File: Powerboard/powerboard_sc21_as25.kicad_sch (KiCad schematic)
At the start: 56 parts, among them J2 Conn_01x02_Male, J3 Conn_01x02_Male, J4 Conn_01x08_Male, J9 Conn_Coaxial, Q6 MMDT2222A, Q7 RSJ250P10TL, Q8 RSJ250P10TL, U1 LTC4412xS6, U2 SN65HVD230, U3 ESP32-PICO-D4

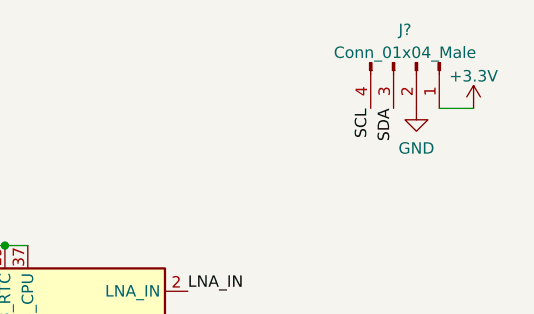
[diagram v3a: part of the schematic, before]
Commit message: assigned FPs for ceramic caps & most resistors
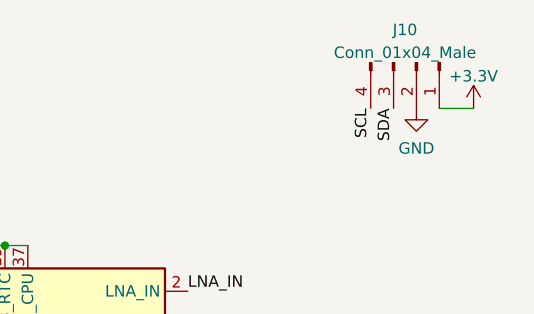
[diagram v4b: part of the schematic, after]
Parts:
- C17, C18, C2, C22, C24: footprint (none) -> Capacitor_SMD:C_0603_1608Metric
- Q7, Q8: footprint RSJ151P10TL -> (none)
- R11, R12, R13, R19, R21, R4, R6, R8: footprint (none) -> Resistor_SMD:R_0603_1608Metric
- R26, R27: footprint Resistor_SMD:R_0805_2012Metric -> Resistor_SMD:R_0603_1608Metric
- gave numbers to parts that had none: 1

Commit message: All capacitors selected, most other footprints assigned
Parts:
- C22: footprint Capacitor_SMD:C_0603_1608Metric -> Capacitor_SMD:C_0805_2012Metric
- Q7, Q8: footprint (none) -> Package_TO_SOT_SMD:TO-263-3_TabPin2

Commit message: Finished footprint assignment
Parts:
- J10: footprint (none) -> Connector_JST:JST_XH_B4B-XH-AM_1x04_P2.50mm_Vertical
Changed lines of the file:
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@@
     (property "Reference" "J10" (id 0) (at 261.62 9.051 90))
     (property "Value" "Conn_01x04_Male" (id 1) (at 261.62 11.5879 90))
-    (property "Footprint" "" (id 2) (at 262.89 12.7 0)
+    (property "Footprint" "Connector_JST:JST_XH_B4B-XH-AM_1x04_P2.50mm_Vertical" (id 2) (at 262.89 12.7 0)
       (effects (font (size 1.27 1.27)) hide)
     )
@@
       (reference "D4") (unit 1) (value "SM712_SOT23") (footprint "Package_TO_SOT_SMD:SOT-23")
     )
-    (path "/00000000-0000-0000-0000-000061f04c1a/00000000-0000-0000-0000-0000621dc1f9"
-      (reference "D5") (unit 1) (value "MBRD835LT4G-iclr") (footprint "")
-    )
-    (path "/00000000-0000-0000-0000-000061f04c1a/00000000-0000-0000-0000-00006213cd52"
-      (reference "D6") (unit 1) (value "MBRD835LT4G-iclr") (footprint "")
+    (path "/00000000-0000-0000-0000-000061f04c1a/168647c2-484c-407b-b4ac-18965f55a420"
+      (reference "D5") (unit 1) (value "DST1550S") (footprint "Package_TO_SOT_SMD:TO-277B")
+    )
+    (path "/00000000-0000-0000-0000-000061f04c1a/a109042f-1ea1-4841-be36-f43dde37235d"
+      (reference "D6") (unit 1) (value "DST1550S") (footprint "Package_TO_SOT_SMD:TO-277B")
     )
     (path "/b1853ee1-af2e-49ab-93e4-e29b2d9f793d/200427ad-2832-4dbb-9227-2f456bd31af2"
@@
     )
     (path "/00000000-0000-0000-0000-000061beb629/00000000-0000-0000-0000-000061c1bdf7"
-      (reference "J1") (unit 1) (value "Thermistor Connection 103AT NTC") (footprint "")
+      (reference "J1") (unit 1) (value "Thermistor Connection 103AT NTC") (footprint "Connector_JST:JST_XH_B2B-XH-AM_1x02_P2.50mm_Vertical")
     )
     (path "/c8adaee4-a569-4b26-9704-a76aac17e42f"
@@
     )
     (path "/2bb15f4e-d587-4e21-952d-752ef72a3b28"
-      (reference "J10") (unit 1) (value "Conn_01x04_Male") (footprint "")
+      (reference "J10") (unit 1) (value "Conn_01x04_Male") (footprint "Connector_JST:JST_XH_B4B-XH-AM_1x04_P2.50mm_Vertical")
     )
     (path "/a9c6c562-c597-48be-b814-c3219c333b03"
@@
     )
     (path "/00000000-0000-0000-0000-000061beb629/00000000-0000-0000-0000-000061c2a952"
-      (reference "L1") (unit 1) (value "6.8µH") (footprint "")
+      (reference "L1") (unit 1) (value "6.8µH") (footprint "iclr:INDM8681X400N")
     )
     (path "/00000000-0000-0000-0000-000061f04c1a/00000000-0000-0000-0000-0000621dae9b"
-      (reference "L3") (unit 1) (value "15uH") (footprint "")
+      (reference "L3") (unit 1) (value "15uH") (footprint "Inductor_SMD:L_12x12mm_H8mm")
     )
     (path "/00000000-0000-0000-0000-000061f04c1a/00000000-0000-0000-0000-00006213b3a4"
-      (reference "L4") (unit 1) (value "15uH") (footprint "")
+      (reference "L4") (unit 1) (value "15uH") (footprint "Inductor_SMD:L_12x12mm_H8mm")
     )
     (path "/00000000-0000-0000-0000-000061beb629/d4dbc84e-5259-40bb-b548-8c4c2e8f188e"
@@
     )
     (path "/00000000-0000-0000-0000-000061beb629/00000000-0000-0000-0000-000061c1bf7d"
-      (reference "R20") (unit 1) (value "2Ω") (footprint "")
+      (reference "R20") (unit 1) (value "2Ω") (footprint "Resistor_SMD:R_0603_1608Metric")
     )
     (path "/041ac0f4-5d33-46c7-b0c5-16599efe9d48"
@@
     )
     (path "/00000000-0000-0000-0000-000061beb629/94d4bcbc-d0b4-4890-bd2f-1938da9976a6"
-      (reference "R28") (unit 1) (value "3.5k") (footprint "")
+      (reference "R28") (unit 1) (value "3.5k") (footprint "Resistor_SMD:R_0603_1608Metric")
     )
     (path "/00000000-0000-0000-0000-000061beb629/7c8d90cb-718e-4369-9385-d843337ae655"
-      (reference "R29") (unit 1) (value "3.5k") (footprint "")
+      (reference "R29") (unit 1) (value "3.5k") (footprint "Resistor_SMD:R_0603_1608Metric")
     )
     (path "/00000000-0000-0000-0000-000061beb629/c4a442e2-c6ea-4d2c-bbac-c20e4af8174f"
-      (reference "R30") (unit 1) (value "75k") (footprint "")
+      (reference "R30") (unit 1) (value "75k") (footprint "Resistor_SMD:R_0603_1608Metric")
     )
     (path "/00000000-0000-0000-0000-000061beb629/c915eb51-0839-4c80-9257-72d67559642c"
-      (reference "R31") (unit 1) (value "10k") (footprint "")
+      (reference "R31") (unit 1) (value "10k") (footprint "Resistor_SMD:R_0603_1608Metric")
     )
     (path "/00000000-0000-0000-0000-000061beb629/00000000-0000-0000-0000-000061c1bfdb"
-      (reference "R32") (unit 1) (value "1kΩ") (footprint "")
+      (reference "R32") (unit 1) (value "1kΩ") (footprint "Resistor_SMD:R_0603_1608Metric")
     )
     (path "/b1853ee1-af2e-49ab-93e4-e29b2d9f793d/a97adbbf-7a4b-4c74-8340-d0fb219e42dc"
-      (reference "R35") (unit 1) (value "5.1k") (footprint "")
+      (reference "R35") (unit 1) (value "5.1k") (footprint "Resistor_SMD:R_0603_1608Metric")
     )
     (path "/b1853ee1-af2e-49ab-93e4-e29b2d9f793d/bcc5df80-5ff7-4cd0-ab07-1de903427559"
-      (reference "R36") (unit 1) (value "5.1k") (footprint "")
+      (reference "R36") (unit 1) (value "5.1k") (footprint "Resistor_SMD:R_0603_1608Metric")
     )
     (path "/b1853ee1-af2e-49ab-93e4-e29b2d9f793d/8a2eb8c1-edca-494b-bd42-22be2f4b411e"
-      (reference "R37") (unit 1) (value "470Ω") (footprint "")
+      (reference "R37") (unit 1) (value "470Ω") (footprint "Resistor_SMD:R_0603_1608Metric")
     )
     (path "/b1853ee1-af2e-49ab-93e4-e29b2d9f793d/7e3b3cf8-4aae-4b66-854b-9074464bdcac"
-      (reference "R38") (unit 1) (value "24k") (footprint "")
+      (reference "R38") (unit 1) (value "24k") (footprint "Resistor_SMD:R_0603_1608Metric")
     )
     (path "/b1853ee1-af2e-49ab-93e4-e29b2d9f793d/3fdc1205-170d-4bad-a583-c2274b810ac0"
-      (reference "R39") (unit 1) (value "47k") (footprint "")
+      (reference "R39") (unit 1) (value "47k") (footprint "Resistor_SMD:R_0603_1608Metric")
     )
     (path "/b1853ee1-af2e-49ab-93e4-e29b2d9f793d/fafc9743-de90-4f11-86ef-3c831f0e7b56"
-      (reference "R40") (unit 1) (value "4.7k") (footprint "")
+      (reference "R40") (unit 1) (value "4.7k") (footprint "Resistor_SMD:R_0603_1608Metric")
     )
     (path "/b1853ee1-af2e-49ab-93e4-e29b2d9f793d/a6bf9111-8852-4077-bff6-579c92450f65"
@@
     )
     (path "/00000000-0000-0000-0000-000061beb629/00000000-0000-0000-0000-000061c1bdbb"
-      (reference "RAC1") (unit 1) (value "10mΩ") (footprint "")
+      (reference "RAC1") (unit 1) (value "10mΩ") (footprint "Resistor_SMD:R_0603_1608Metric")
     )
     (path "/00000000-0000-0000-0000-000061beb629/00000000-0000-0000-0000-000061c1be29"
-      (reference "RAdp1") (unit 1) (value "150kΩ") (footprint "")
+      (reference "RAdp1") (unit 1) (value "150kΩ") (footprint "Resistor_SMD:R_0603_1608Metric")
     )
     (path "/00000000-0000-0000-0000-000061beb629/00000000-0000-0000-0000-000061c1be23"
-      (reference "RFast1") (unit 1) (value "32kΩ") (footprint "")
+      (reference "RFast1") (unit 1) (value "32kΩ") (footprint "Resistor_SMD:R_0603_1608Metric")
     )
     (path "/00000000-0000-0000-0000-000061beb629/00000000-0000-0000-0000-000061c1be2f"
-      (reference "RPre1") (unit 1) (value "13kΩ") (footprint "")
+      (reference "RPre1") (unit 1) (value "13kΩ") (footprint "Resistor_SMD:R_0603_1608Metric")
     )
     (path "/00000000-0000-0000-0000-000061beb629/00000000-0000-0000-0000-000061c2a94c"
-      (reference "RSR1") (unit 1) (value "10mΩ") (footprint "")
+      (reference "RSR1") (unit 1) (value "10mΩ") (footprint "Resistor_SMD:R_0603_1608Metric")
     )
     (path "/00000000-0000-0000-0000-0000620bb99a"
